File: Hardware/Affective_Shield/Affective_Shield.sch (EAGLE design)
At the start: 17 parts

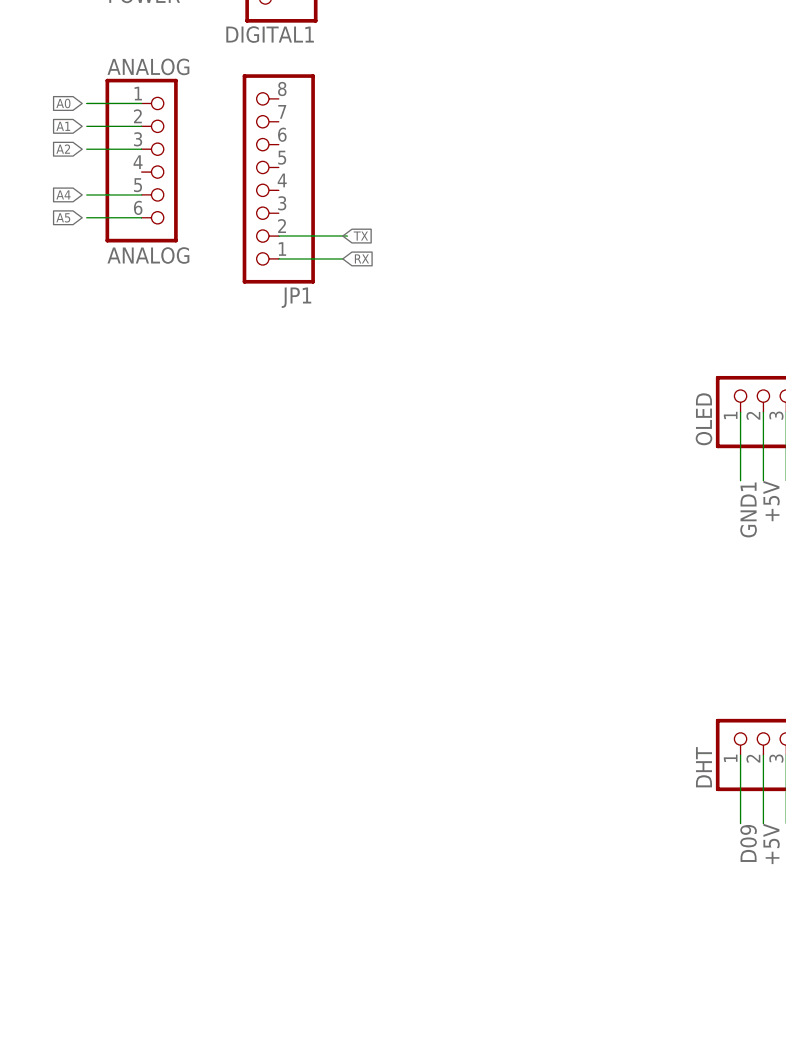
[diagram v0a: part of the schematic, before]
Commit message: Add Oximetry and GPS
Oximetry sensor added. GPS added
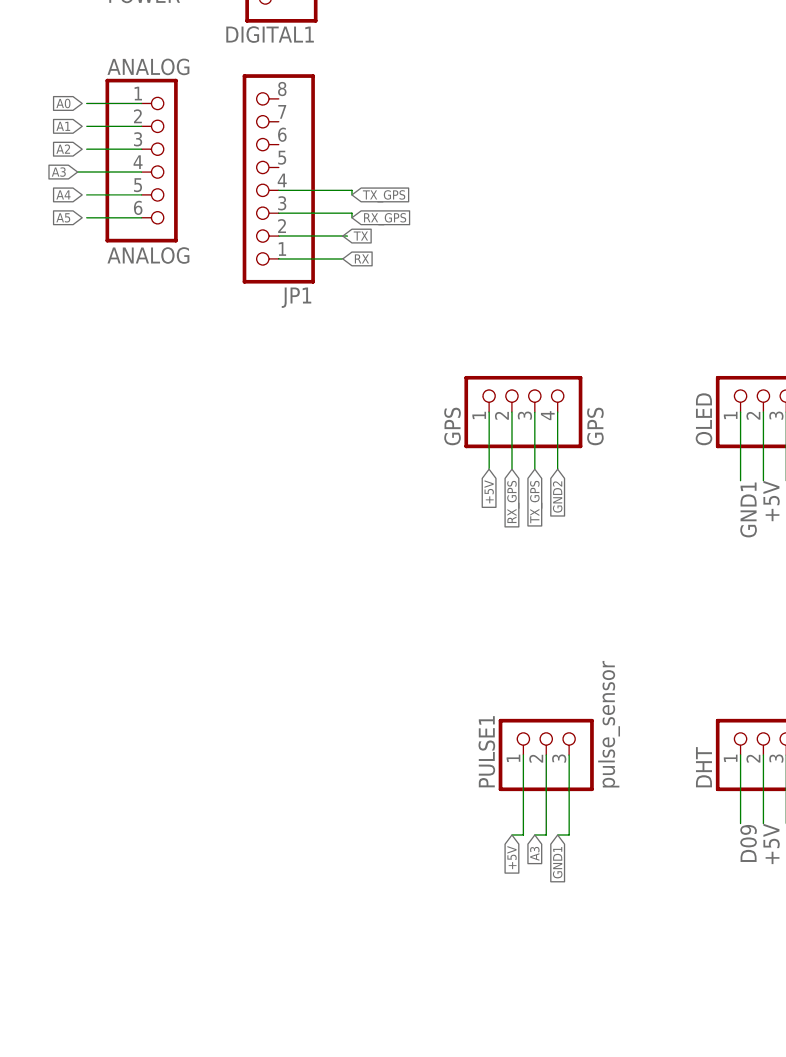
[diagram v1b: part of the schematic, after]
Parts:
- added GPS: GPS, pinhead:PINHD-1X4
- added PULSE1: pulse_sensor, pinhead:PINHD-1X3
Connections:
- new net A3: ANALOG.4, PULSE1.2
- new net RX_GPS: GPS.2, JP1.3
- new net TX_GPS: GPS.3, JP1.4
- net +5V: now also GPS.1, PULSE1.1
- net GND1: now also PULSE1.3
- net GND2: now also GPS.4
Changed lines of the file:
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@@
 <?xml version="1.0" encoding="utf-8"?>
 <!DOCTYPE eagle SYSTEM "eagle.dtd">
-<eagle version="8.4.2">
+<eagle version="9.0.0">
 <drawing>
 <settings>
@@
 <part name="ANALOG" library="pinhead" library_urn="urn:adsk.eagle:library:325" deviceset="PINHD-1X6" device="" package3d_urn="urn:adsk.eagle:package:22472/2" value="ANALOG"/>
 <part name="JP1" library="pinhead" library_urn="urn:adsk.eagle:library:325" deviceset="PINHD-1X8" device="" package3d_urn="urn:adsk.eagle:package:22409/2"/>
+<part name="GPS" library="pinhead" library_urn="urn:adsk.eagle:library:325" deviceset="PINHD-1X4" device="" package3d_urn="urn:adsk.eagle:package:22407/2" value="GPS"/>
+<part name="PULSE1" library="pinhead" library_urn="urn:adsk.eagle:library:325" deviceset="PINHD-1X3" device="" package3d_urn="urn:adsk.eagle:package:22458/2" value="pulse_sensor"/>
 </parts>
 <sheets>
@@
 <instance part="ANALOG" gate="A" x="19.812" y="137.16"/>
 <instance part="JP1" gate="A" x="29.972" y="137.668" rot="R180"/>
+<instance part="GPS" gate="A" x="60.96" y="113.03" rot="R90"/>
+<instance part="PULSE1" gate="A" x="62.23" y="74.93" rot="R90"/>
 </instances>
 <busses>
@@
 <label x="10.16" y="168.656" size="1.016" layer="95" rot="R180" xref="yes"/>
 </segment>
+<segment>
+<pinref part="GPS" gate="A" pin="1"/>
+<wire x1="55.88" y1="110.49" x2="55.88" y2="104.14" width="0.1524" layer="91"/>
+<label x="55.88" y="104.14" size="1.016" layer="95" rot="R270" xref="yes"/>
+</segment>
+<segment>
+<pinref part="PULSE1" gate="A" pin="1"/>
+<wire x1="59.69" y1="72.39" x2="59.69" y2="63.5" width="0.1524" layer="91"/>
+<wire x1="59.69" y1="63.5" x2="58.42" y2="63.5" width="0.1524" layer="91"/>
+<label x="58.42" y="63.5" size="1.016" layer="95" rot="R270" xref="yes"/>
+</segment>
 </net>
 <net name="D09" class="0">
@@
 <label x="40.64" y="171.704" size="1.016" layer="95" xref="yes"/>
 </segment>
+<segment>
+<pinref part="GPS" gate="A" pin="4"/>
+<wire x1="63.5" y1="110.49" x2="63.5" y2="104.14" width="0.1524" layer="91"/>
+<label x="63.5" y="104.14" size="1.016" layer="95" rot="R270" xref="yes"/>
+</segment>
 </net>
 <net name="GND1" class="0">
@@
 <label x="10.16" y="166.116" size="1.016" layer="95" rot="R180" xref="yes"/>
 </segment>
-</net>
+<segment>
+<pinref part="PULSE1" gate="A" pin="3"/>
+<wire x1="64.77" y1="72.39" x2="64.77" y2="63.5" width="0.1524" layer="91"/>
+<wire x1="64.77" y1="63.5" x2="63.5" y2="63.5" width="0.1524" layer="91"/>
+<label x="63.5" y="63.5" size="1.016" layer="95" rot="R270" xref="yes"/>
+</segment>
+</net>
+<net name="TX_GPS" class="0">
+<segment>
+<pinref part="JP1" gate="A" pin="4"/>
+<wire x1="32.512" y1="135.128" x2="40.64" y2="135.128" width="0.1524" layer="91"/>
+<wire x1="40.64" y1="135.128" x2="40.64" y2="134.62" width="0.1524" layer="91"/>
+<label x="40.64" y="134.62" size="1.016" layer="95" xref="yes"/>
+</segment>
+<segment>
+<pinref part="GPS" gate="A" pin="3"/>
+<wire x1="60.96" y1="110.49" x2="60.96" y2="104.14" width="0.1524" layer="91"/>
+<label x="60.96" y="104.14" size="1.016" layer="95" rot="R270" xref="yes"/>
+</segment>
+</net>
+<net name="RX_GPS" class="0">
+<segment>
+<pinref part="JP1" gate="A" pin="3"/>
+<wire x1="32.512" y1="132.588" x2="40.64" y2="132.588" width="0.1524" layer="91"/>
+<wire x1="40.64" y1="132.588" x2="40.64" y2="132.08" width="0.1524" layer="91"/>
+<label x="40.64" y="132.08" size="1.016" layer="95" xref="yes"/>
+</segment>
+<segment>
+<pinref part="GPS" gate="A" pin="2"/>
+<wire x1="58.42" y1="110.49" x2="58.42" y2="104.14" width="0.1524" layer="91"/>
+<label x="58.42" y="104.14" size="1.016" layer="95" rot="R270" xref="yes"/>
+</segment>
+</net>
+<net name="A3" class="0">
+<segment>
+<pinref part="PULSE1" gate="A" pin="2"/>
+<wire x1="62.23" y1="72.39" x2="62.23" y2="63.5" width="0.1524" layer="91"/>
+<wire x1="62.23" y1="63.5" x2="60.96" y2="63.5" width="0.1524" layer="91"/>
+<label x="60.96" y="63.5" size="1.016" layer="95" rot="R270" xref="yes"/>
+</segment>
+<segment>
+<pinref part="ANALOG" gate="A" pin="4"/>
+<wire x1="17.272" y1="137.16" x2="10.16" y2="137.16" width="0.1524" layer="91"/>
+<label x="10.16" y="137.16" size="1.016" layer="95" rot="R180" xref="yes"/>
+</segment>
+</net>

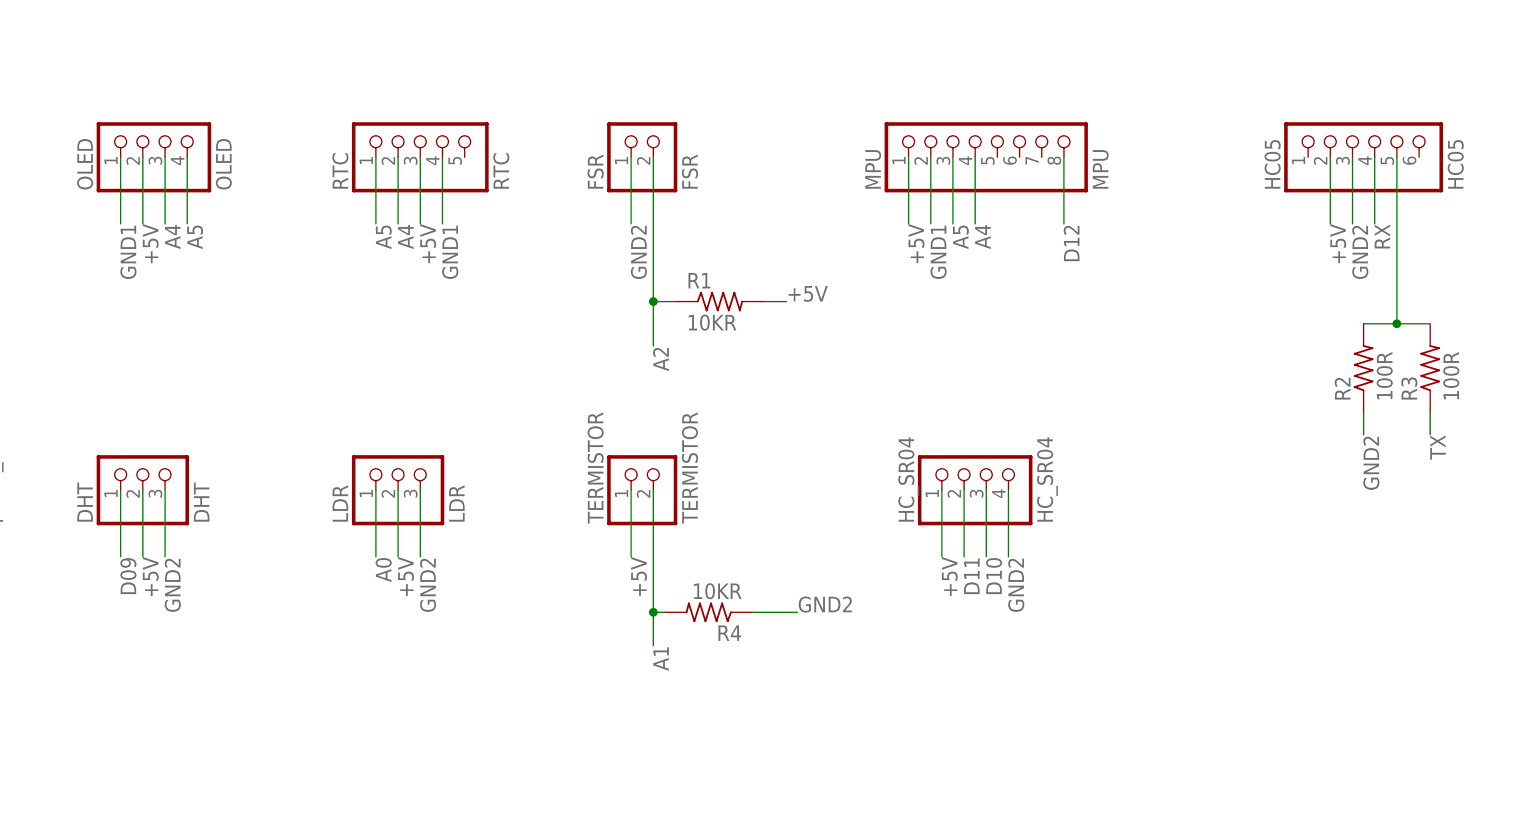
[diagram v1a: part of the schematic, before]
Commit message: shield corrective update: Changed some ports, and adapted to only bottom solder on components
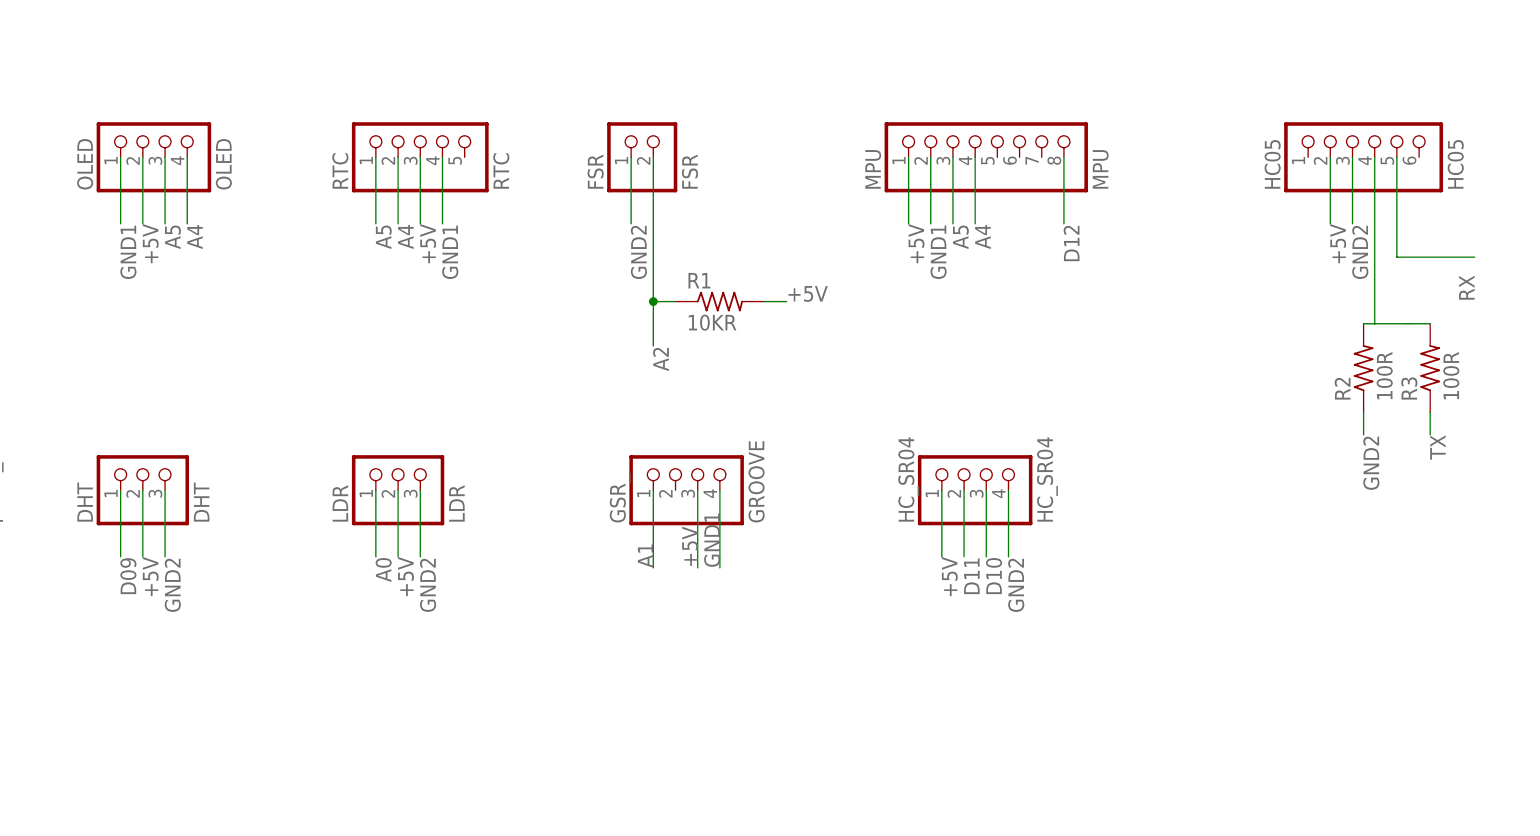
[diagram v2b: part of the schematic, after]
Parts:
- removed R4: 10KR, resistor:R-US_0204/7
- removed TERMISTOR: TERMISTOR, pinhead:PINHD-1X2
- added GSR_: GROOVE, pinhead:PINHD-1X4
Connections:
- net +5V: now also GSR_.3; no longer TERMISTOR.1
- net A1: now also GSR_.1; no longer R4.2, TERMISTOR.2
- net A4: now also OLED.4; no longer OLED.3
- net A5: now also OLED.3; no longer OLED.4
- net GND1: now also GSR_.4
- net GND2: no longer R4.1
- net N$3: now also HC05.4; no longer HC05.5
- net RX: now also HC05.5; no longer HC05.4
